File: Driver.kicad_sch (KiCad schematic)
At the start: 18 parts, among them J1 Screw_Terminal_01x05, U1 IS31FL3239, U2 AP2204K-ADJ

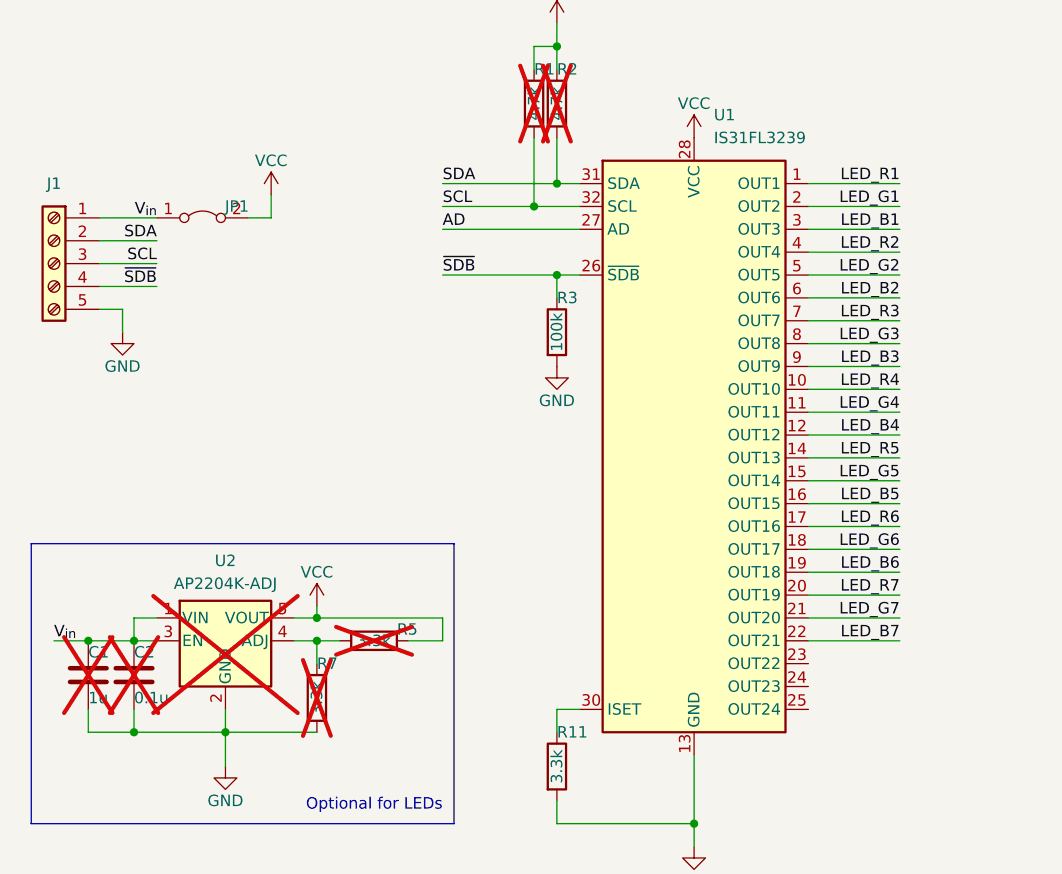
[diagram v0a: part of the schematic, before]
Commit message: PCB shows no errors, needs improvements before prototype
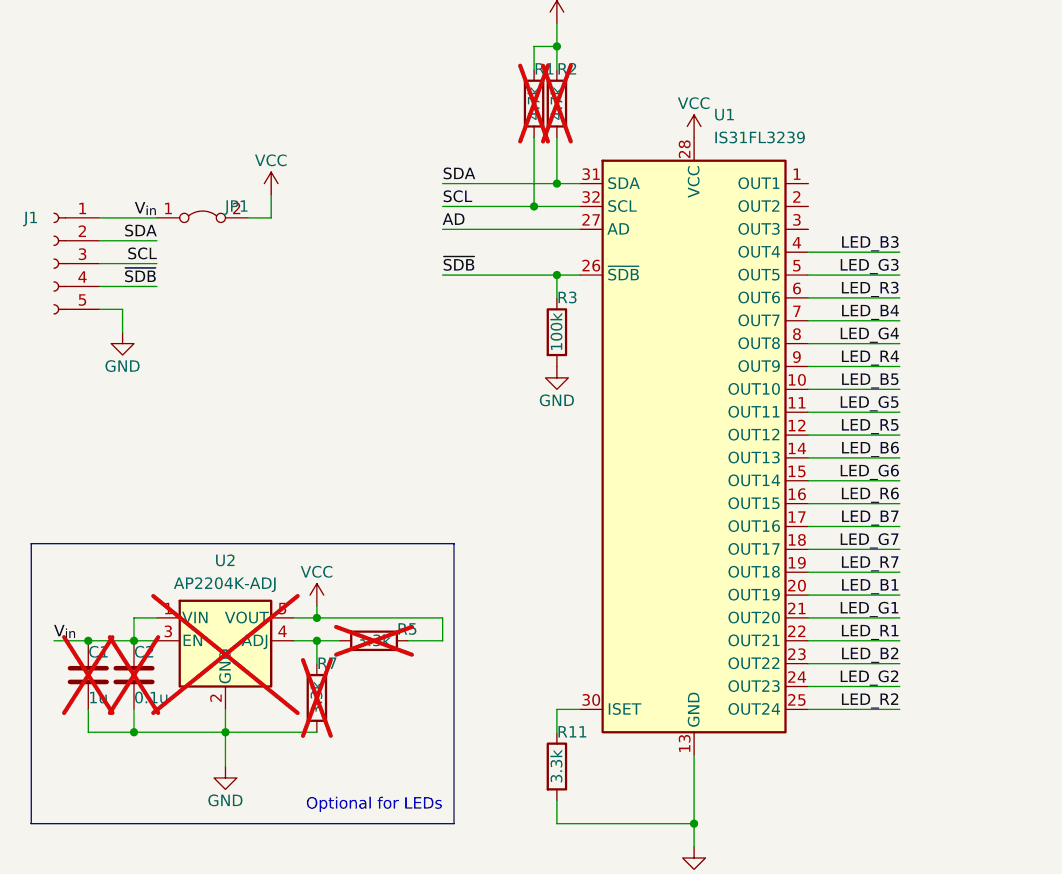
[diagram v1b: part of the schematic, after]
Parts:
- removed J1: Screw_Terminal_01x05, TerminalBlock_Phoenix:TerminalBlock_Phoenix_MKDS-1,5-5_1x05_P5.00mm_Horizontal, symbol Connector:Screw_Terminal_01x05
- added J1: Conn_01x05_Socket, Connector_PinHeader_2.54mm:PinHeader_1x05_P2.54mm_Vertical, symbol Connector:Conn_01x05_Socket
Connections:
- net GND: now also J1.5 (Pin_5)
- net LED_B1: now also U1.20 (OUT19); no longer U1.3 (OUT3)
- net LED_B2: now also U1.23 (OUT22); no longer U1.6 (OUT6)
- net LED_B3: now also U1.4 (OUT4); no longer U1.9 (OUT9)
- net LED_B4: now also U1.7 (OUT7); no longer U1.12 (OUT12)
- net LED_B5: now also U1.10 (OUT10); no longer U1.16 (OUT15)
- net LED_B6: now also U1.14 (OUT13); no longer U1.19 (OUT18)
- net LED_B7: now also U1.17 (OUT16); no longer U1.22 (OUT21)
- net LED_G1: now also U1.21 (OUT20); no longer U1.2 (OUT2)
- net LED_G2: now also U1.24 (OUT23); no longer U1.5 (OUT5)
- net LED_G3: now also U1.5 (OUT5); no longer U1.8 (OUT8)
- net LED_G4: now also U1.8 (OUT8); no longer U1.11 (OUT11)
- net LED_G5: now also U1.11 (OUT11); no longer U1.15 (OUT14)
- net LED_G6: now also U1.15 (OUT14); no longer U1.18 (OUT17)
- net LED_G7: now also U1.18 (OUT17); no longer U1.21 (OUT20)
- net LED_R1: now also U1.22 (OUT21); no longer U1.1 (OUT1)
- net LED_R2: now also U1.25 (OUT24); no longer U1.4 (OUT4)
- net LED_R3: now also U1.6 (OUT6); no longer U1.7 (OUT7)
- net LED_R4: now also U1.9 (OUT9); no longer U1.10 (OUT10)
- net LED_R5: now also U1.12 (OUT12); no longer U1.14 (OUT13)
- net LED_R6: now also U1.16 (OUT15); no longer U1.17 (OUT16)
- net LED_R7: now also U1.19 (OUT18); no longer U1.20 (OUT19)
- net SCL: now also J1.3 (Pin_3)
- net SDA: now also J1.2 (Pin_2)
- net V_{in}: now also J1.1 (Pin_1)
- net ~{SDB}: now also J1.4 (Pin_4)

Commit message: More updates/work. Close to finished board
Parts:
- removed C1: 1u, Capacitor_SMD:C_0805_2012Metric_Pad1.18x1.45mm_HandSolder, symbol Device:C
- removed C2: 0.1u, Capacitor_SMD:C_0805_2012Metric_Pad1.18x1.45mm_HandSolder, symbol Device:C
- removed JP1: Jumper_2_Bridged, Jumper:SolderJumper-2_P1.3mm_Bridged_RoundedPad1.0x1.5mm, symbol Jumper:Jumper_2_Bridged
- removed R7: 3.3k, Resistor_SMD:R_0805_2012Metric_Pad1.20x1.40mm_HandSolder, symbol Device:R
- removed U2: AP2204K-ADJ, Package_TO_SOT_SMD:SOT-23-5, symbol Regulator_Linear:AP2204K-ADJ
- added J2: Conn_01x05_Socket, ProjectLibrary:CustomBoardInterconnectMirror, symbol Connector:Conn_01x05_Socket
- added J3: Conn_01x05_Pin, ProjectLibrary:CustomBoardInterconnect, symbol Connector:Conn_01x05_Pin
- added R6: 0, Resistor_SMD:R_0805_2012Metric_Pad1.20x1.40mm_HandSolder, symbol Device:R
- R5: value 3.3k -> 0
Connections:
- net V_{in} is gone; now on net VCC: J1.1 (Pin_1)
- net AD: now also R5.2, R6.2
- net GND: now also J1.4 (Pin_4), J2.2 (Pin_2), J3.2 (Pin_2); no longer J1.5 (Pin_5)
- net SCL: now also J2.3 (Pin_3), J3.3 (Pin_3), R6.1
- net SDA: now also R5.1, J2.4 (Pin_4), J3.4 (Pin_4)
- net VCC: now also J2.5 (Pin_5), J3.5 (Pin_5); no longer R5.1
- net ~{SDB}: now also J1.5 (Pin_5), J2.1 (Pin_1), J3.1 (Pin_1); no longer J1.4 (Pin_4)
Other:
- note removed: "Optional for LEDs"
- moved on the sheet: R4
